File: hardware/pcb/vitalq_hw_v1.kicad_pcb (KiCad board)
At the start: 4 copper layers, 37 x 30 mm, 86 parts, among them J1 USB-C, J2 LiPo pads, J3 FSR pads, J4 PPG pads, J5 ECG pads, J6 EDA pads, U1 ESP32-WROOM-32E-N8R2, U10 AS7341-DLGM, U11 TMP117AIDRVR, U12 MLX90632SLD-DCB-100-SP, U13 BME280, U14 LSM6DSV80XTR, U2 MCP73831T-2ACI/OT, U3 XC6206P332MR-G, U4 TPS7A2018PDBVR, U5 CP2102N-A02-GQFN28R, U6 AFE4900YZR, U7 AD5940BCBZ-RL7, U8 ADS1292RIRSMT, U9 PCA9306DCUR

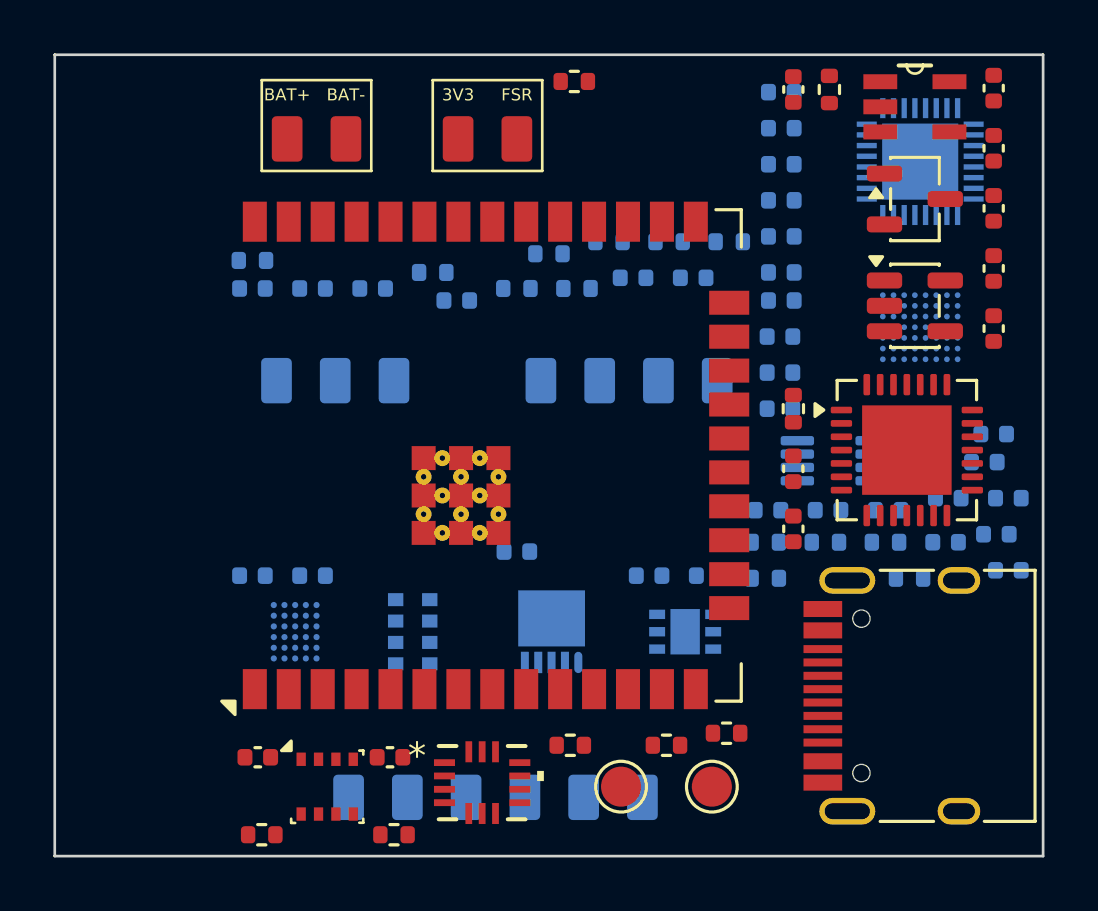
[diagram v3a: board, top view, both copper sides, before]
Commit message: Pack the hw_v1 board to 36.2 x 28 mm and correct the 3D models.
The LSM6 body is a 3.0 x 2.5 x 0.83 mm box in KiCad VRML units, and the other vendor models are rotated so they stand on their lands. Skin sensors sit in one bottom cluster with the electrode pads around them, bypass parts are packed next to their ICs outside the antenna keep-out, and the schematic frames clear the title block.

Co-authored-by: Riyu-D1 <Riyu-D1@users.noreply.github.com>
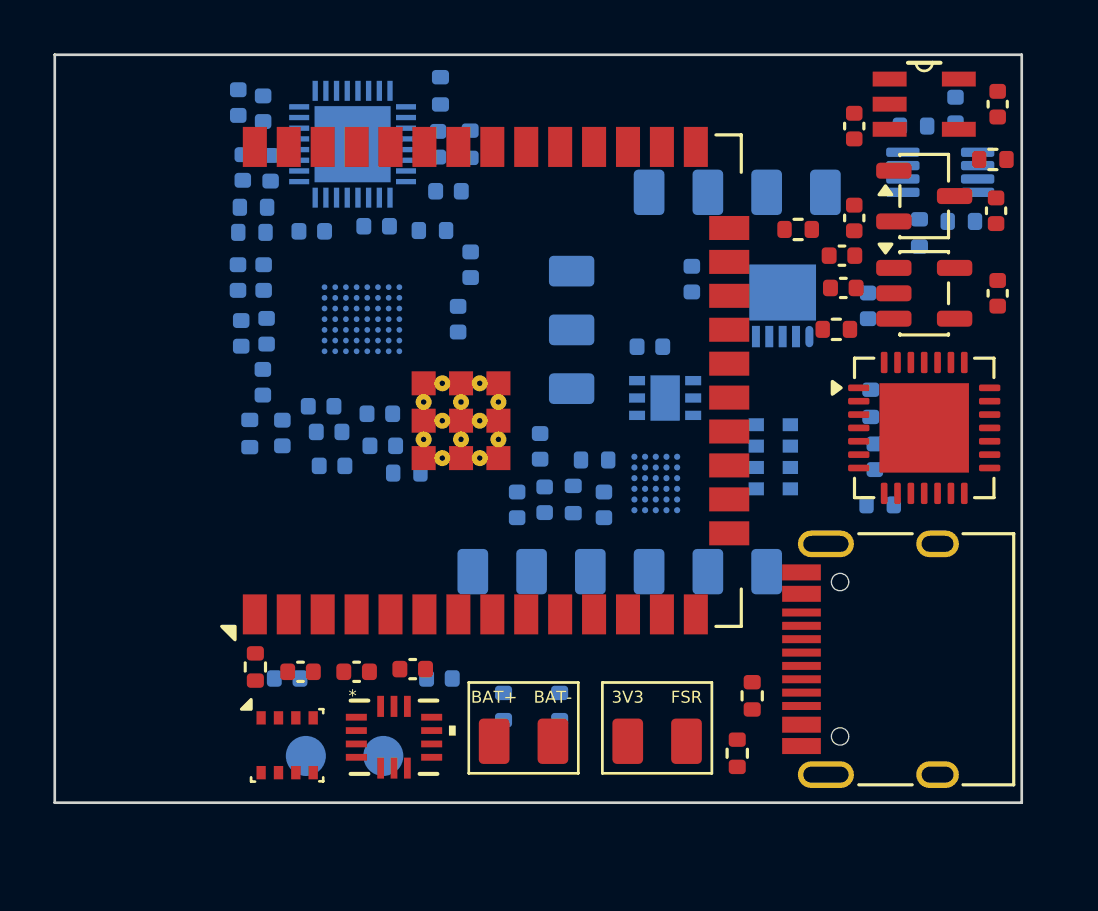
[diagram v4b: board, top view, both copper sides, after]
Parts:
- R6, R7, TP1, TP2: moved to B.Cu
- moved C20 30.0 mm to (7.82, 8.34), turned to 90 degrees
- moved C25 27.8 mm to (6.86, 8.34), turned to 90 degrees
- moved C26 27.3 mm to (8.52, 14.2), turned to 90 degrees
- moved R8 25.9 mm to (25.6, 26.1), turned to 90 degrees
- moved C21 25.3 mm to (10.3, 14.1)
- moved C5 25.2 mm to (13.4, 23.0), turned to 0 degrees
- moved R2 25.1 mm to (29.3, 10.3)
- moved J2 23.8 mm to (17.6, 25.7)
- moved J3 23.4 mm to (22.6, 25.7)
- moved C41 23.3 mm to (33.7, 2.07), turned to 90 degrees
- moved C38 23.1 mm to (30.4, 9.40), turned to 90 degrees
- moved C23 22.9 mm to (6.98, 10.4), turned to 90 degrees
- moved C27 22.2 mm to (10.4, 15.4)
- moved U8 21.3 mm to (11.2, 3.35)
- moved U7 20.9 mm to (11.5, 9.90)
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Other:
- board size 37 x 30 mm -> 36.2 x 28 mm

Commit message: Seat the QFN models and drop passives the datasheets do not require.
The ADS1292R STEP is already Z-up, so the extra X rotation stood the
4x4x1 mm body on edge. Remove TP1, TP2, C5, C12, C17, C31 and R4, add
the 1 uF AVDD bulk capacitor, and shorten the outline to 36.2 x 27.8 mm.

Co-authored-by: Riyu-D1 <Riyu-D1@users.noreply.github.com>
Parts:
- removed C12, C17, C31: 100n, Capacitor_SMD:C_0402_1005Metric
- removed C5: 1u, Capacitor_SMD:C_0402_1005Metric
- removed R4: 1k, Resistor_SMD:R_0402_1005Metric
- removed TP1: EN, TestPoint:TestPoint_Pad_D1.5mm
- removed TP2: IO0, TestPoint:TestPoint_Pad_D1.5mm
- added C43: 1u, Capacitor_SMD:C_0402_1005Metric, B.Cu at (12.1, 6.42)
- moved R16 4.41 mm to (17.2, 3.40)
- moved C29 2.10 mm to (14.1, 6.58)
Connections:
- U5 pad 9: CP_RST -> unconnected-(U5-~{RST}-Pad9)
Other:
- board size 36.2 x 28 mm -> 36.2 x 27.8 mm

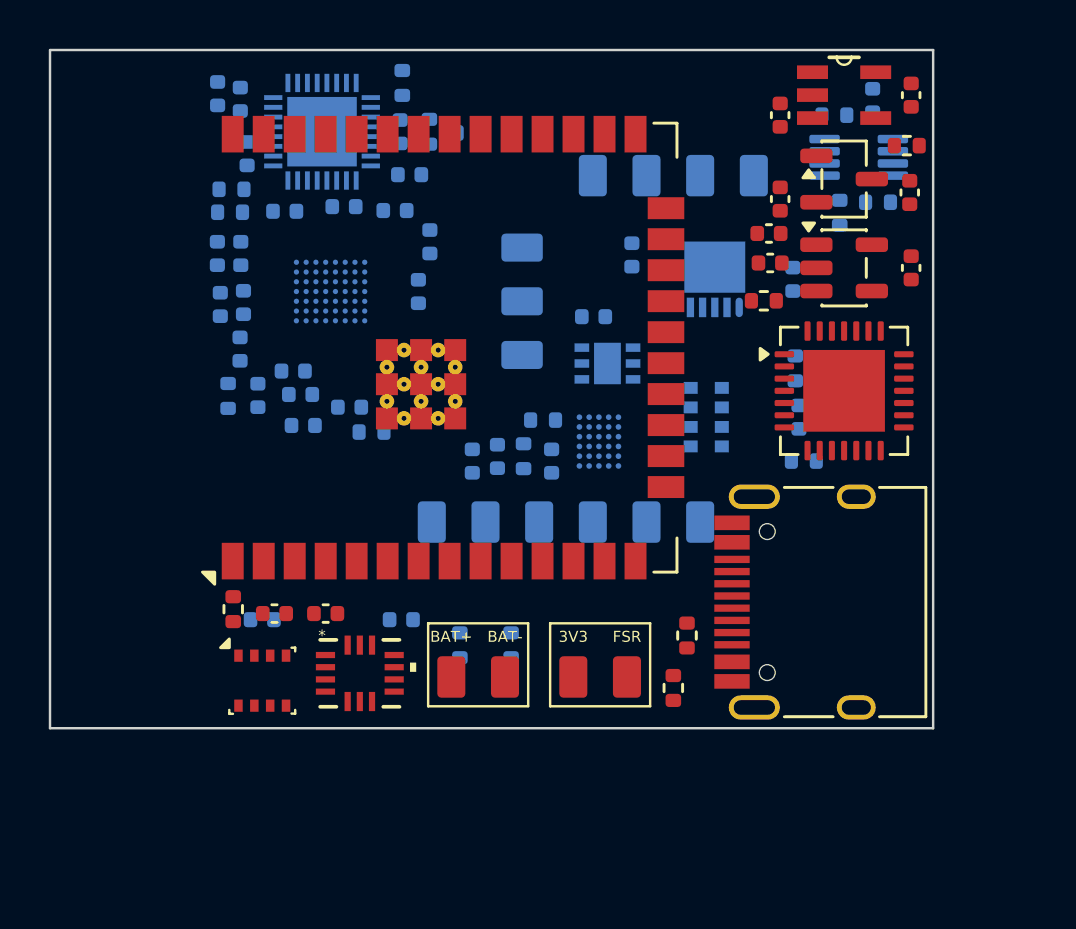
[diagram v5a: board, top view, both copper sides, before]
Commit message: Add the chest-board sensors and replace the 3.3 V LDO with a TPS63802.
The unrouted 40 x 34 mm board keeps every previous part except the off-board PPG pads, which the SFH 7072 replaces. Respiration, a second ECG lead, electrode protection, EDA, fuel gauge, flash, and the I/O expander are in the schematic.

Co-authored-by: Riyu-D1 <Riyu-D1@users.noreply.github.com>
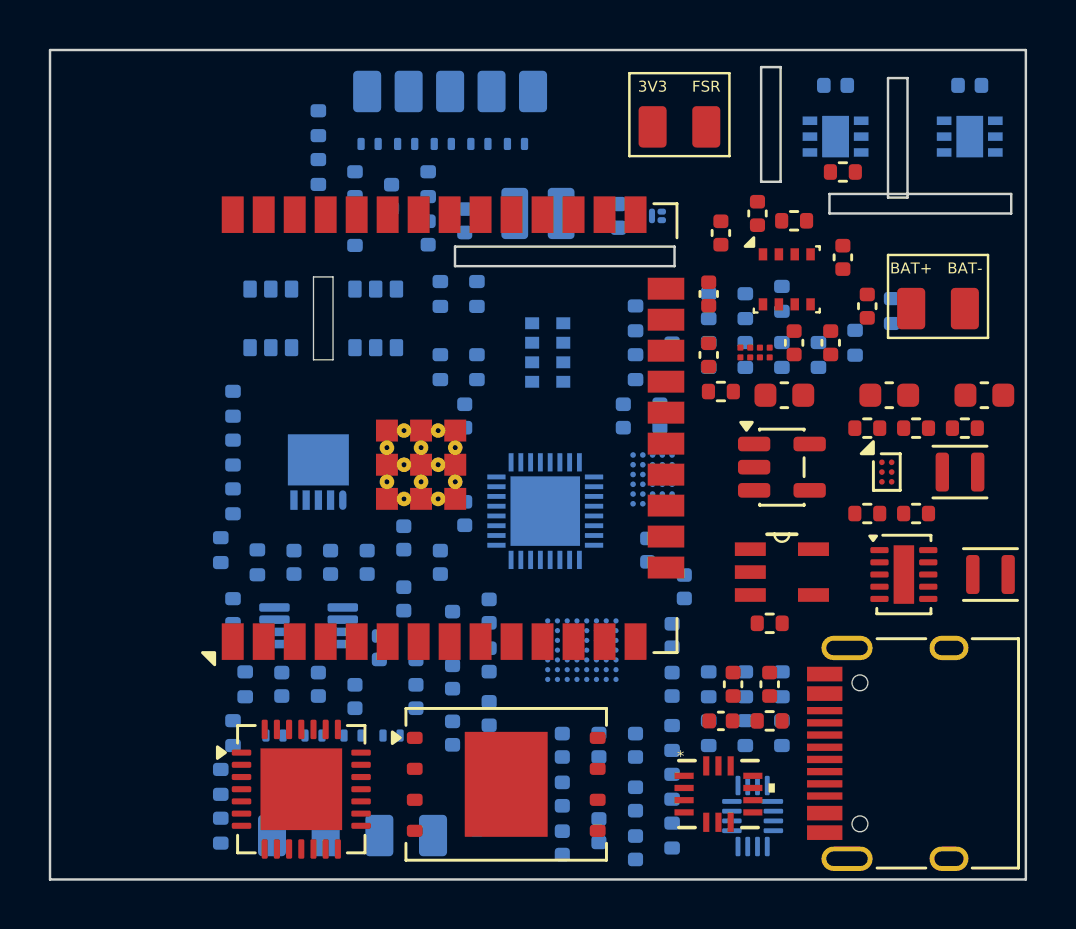
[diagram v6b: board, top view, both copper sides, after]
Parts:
- removed J4: PPG pads, vitalq:Pads_PPG
- added C44: 10u, Capacitor_SMD:C_0603_1608Metric, F.Cu at (30.1, 14.2)
- added C45: 22u, Capacitor_SMD:C_0603_1608Metric, F.Cu at (34.4, 14.2)
- added C46: 2.2u, Capacitor_SMD:C_0402_1005Metric, F.Cu at (32.5, 8.50)
- added C47: 4.7u, Capacitor_SMD:C_0603_1608Metric, F.Cu at (38.3, 14.2)
- added C48: 2.2n, Capacitor_SMD:C_0402_1005Metric, B.Cu at (11.0, 26.0)
- added C49: 2.2n, Capacitor_SMD:C_0402_1005Metric, B.Cu at (12.5, 26.5)
- added C50: 100n, Capacitor_SMD:C_0402_1005Metric, B.Cu at (17.0, 15.0)
- added C51: 100n, Capacitor_SMD:C_0402_1005Metric, B.Cu at (10.0, 21.0)
- added C52: 2.2n, Capacitor_SMD:C_0402_1005Metric, B.Cu at (9.50, 26.0)
- added C53: 2.2n, Capacitor_SMD:C_0402_1005Metric, B.Cu at (22.5, 28.5)
- added C54: 15n, Capacitor_SMD:C_0402_1005Metric, B.Cu at (21.0, 32.5)
- added C55: 470n, Capacitor_SMD:C_0402_1005Metric, B.Cu at (24.0, 28.5)
- added C56: 100n, Capacitor_SMD:C_0402_1005Metric, B.Cu at (25.0, 15.0)
- added C57: 100n, Capacitor_SMD:C_0402_1005Metric, B.Cu at (25.5, 26.0)
- added C58: 100n, Capacitor_SMD:C_0402_1005Metric, F.Cu at (27.5, 7.50)
- added C59: 100n, Capacitor_SMD:C_0402_1005Metric, B.Cu at (24.0, 30.7)
- added C60: 100n, Capacitor_SMD:C_0402_1005Metric, B.Cu at (24.0, 32.7)
- added C61: 100n, Capacitor_SMD:C_0402_1005Metric, B.Cu at (37.7, 1.45)
- added D1: TPD1E10B06, vitalq:TPD1E10B06_DPY, B.Cu at (13.1, 3.85)
- added D10: NF2W757G-F1, vitalq:NF2W757G, B.Cu at (20.0, 6.70)
- added D11: SFH4053, LED_SMD:LED_0402_1005Metric, B.Cu at (23.3, 6.80)
- added D2: TPD1E10B06, vitalq:TPD1E10B06_DPY, B.Cu at (14.6, 3.85)
- added D3: TPD1E10B06, vitalq:TPD1E10B06_DPY, B.Cu at (16.1, 3.85)
- added D4: TPD1E10B06, vitalq:TPD1E10B06_DPY, B.Cu at (17.6, 3.85)
- added D5: TPD1E10B06, vitalq:TPD1E10B06_DPY, B.Cu at (19.1, 3.85)
- added D6: TPD1E10B06, vitalq:TPD1E10B06_DPY, B.Cu at (9.20, 28.1)
- added D7: TPD1E10B06, vitalq:TPD1E10B06_DPY, B.Cu at (10.8, 28.1)
- added D8: TPD1E10B06, vitalq:TPD1E10B06_DPY, B.Cu at (12.4, 28.1)
- added D9: TPD1E10B06, vitalq:TPD1E10B06_DPY, B.Cu at (14.0, 28.1)
- added L1: 0.47u, vitalq:L_DFE201612E, F.Cu at (38.5, 21.5)
- added L2: 1.0u, vitalq:L_DFE201612E, F.Cu at (37.3, 17.3)
- added Q1: CSD13380F3, Package_DFN_QFN:Texas_PicoStar_DFN-3_0.69x0.60mm, B.Cu at (24.9, 6.80)
- added R23: 560k, Resistor_SMD:R_0402_1005Metric, F.Cu at (33.5, 19.0)
- added R24: 100k, Resistor_SMD:R_0402_1005Metric, F.Cu at (35.5, 19.0)
- added R25: 100k, Resistor_SMD:R_0402_1005Metric, F.Cu at (35.5, 15.5)
- added R26: 10M, Resistor_SMD:R_0402_1005Metric, B.Cu at (7.50, 16.5)
- added R27: 10M, Resistor_SMD:R_0402_1005Metric, B.Cu at (7.50, 18.5)
- added R28: 10M, Resistor_SMD:R_0402_1005Metric, B.Cu at (7.50, 23.0)
- added R29: 10M, Resistor_SMD:R_0402_1005Metric, B.Cu at (7.50, 28.0)
- added R30: 40.2k, Resistor_SMD:R_0402_1005Metric, B.Cu at (7.00, 30.0)
- added R31: 40.2k, Resistor_SMD:R_0402_1005Metric, B.Cu at (7.00, 20.5)
- added R32: 49.9k, Resistor_SMD:R_0402_1005Metric, B.Cu at (25.5, 11.5)
- added R33: 49.9k, Resistor_SMD:R_0402_1005Metric, B.Cu at (24.0, 11.0)
- added R34: 49.9k, Resistor_SMD:R_0402_1005Metric, B.Cu at (7.00, 32.0)
- added R35: 49.9k, Resistor_SMD:R_0402_1005Metric, B.Cu at (30.0, 26.0)
- added R36: 49.9k, Resistor_SMD:R_0402_1005Metric, B.Cu at (28.5, 28.0)
- added R39: 1k, Resistor_SMD:R_0402_1005Metric, B.Cu at (30.0, 28.0)
- added R40: 1k, Resistor_SMD:R_0402_1005Metric, B.Cu at (27.0, 12.5)
- added R41: 1k, Resistor_SMD:R_0402_1005Metric, B.Cu at (28.5, 12.5)
- added R42: 1k, Resistor_SMD:R_0402_1005Metric, B.Cu at (30.0, 12.5)
- added R43: 10M, Resistor_SMD:R_0402_1005Metric, B.Cu at (31.5, 12.5)
- added R44: 10M, Resistor_SMD:R_0402_1005Metric, B.Cu at (33.0, 12.0)
- added R45: 10M, Resistor_SMD:R_0402_1005Metric, B.Cu at (27.0, 10.5)
- added R46: 10M, Resistor_SMD:R_0402_1005Metric, B.Cu at (28.5, 10.5)
- added R47: 100, Resistor_SMD:R_0402_1005Metric, B.Cu at (11.0, 3.00)
- added R48: 100k, Resistor_SMD:R_0402_1005Metric, B.Cu at (11.0, 5.00)
- added R49: 10k, Resistor_SMD:R_0402_1005Metric, F.Cu at (27.5, 14.0)
- added R50: 100k, Resistor_SMD:R_0402_1005Metric, F.Cu at (30.5, 7.00)
- added R51: 200k, Resistor_SMD:R_0402_1005Metric, F.Cu at (37.5, 15.5)
- added R52: 10k, Resistor_SMD:R_0402_1005Metric, B.Cu at (34.5, 10.7)
- added R53: 10k, Resistor_SMD:R_0402_1005Metric, B.Cu at (30.0, 10.2)
- added U15: TPS61240YFFR, vitalq:TPS61240_YFF, F.Cu at (34.3, 17.3)
- added U16: SFH 7072, vitalq:SFH7072, B.Cu at (11.2, 11.0)
- added U17: MAX17048G+T10, vitalq:MAX17048_WLP, F.Cu at (28.9, 12.4)
- added U18: W25Q512JVEIQ, vitalq:W25Q512_WSON8, F.Cu at (18.7, 30.1)
- added U19: TCA6408ARSVR, vitalq:TCA6408A_RSV, B.Cu at (28.8, 31.4)
- added U20: TMP117AIDRVR, snap:SON65P200X200X80-7N, B.Cu at (37.7, 3.55)
- C37, C38: moved to F.Cu
- C7, C8, R5: moved to B.Cu
- U3: value XC6206P332MR-G -> TPS63802DLAR; footprint Package_TO_SOT_SMD:SOT-23-3 -> Package_SON:WSON-10-1EP_2x3mm_P0.5mm_EP0.84x2.4mm
- moved J6 30.1 mm to (12.4, 32.2)
- moved U9 29.6 mm to (10.6, 23.6)
- moved C40 28.2 mm to (32.2, 1.45)
- moved U5 27.6 mm to (10.3, 30.3)
- moved U13 27.1 mm to (30.2, 9.40)
- moved C25 25.9 mm to (19.5, 31.0)
- moved C42 25.1 mm to (22.5, 32.0)
- moved C1 24.8 mm to (29.5, 26.0)
- moved J2 24.2 mm to (36.4, 10.6)
- moved C33 23.3 mm to (18.0, 23.0)
- moved J3 22.8 mm to (25.8, 3.15)
- moved C22 22.5 mm to (21.0, 30.5)
- moved R8 22.3 mm to (32.5, 5.00), turned to 0 degrees
- moved C19 21.6 mm to (18.0, 29.5)
- moved R21 21.6 mm to (12.5, 5.50), turned to 90 degrees
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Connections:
- C14 pad 1: VBAT -> TX_5V
- J5 pad 1: IN1P -> ECG1_PAD
- J5 pad 2: IN1N -> ECG2_PAD
- J5 pad 3: RLDOUT -> RLD_PAD
- J6 pad 1: CE0 -> EDA_CE_PAD
- J6 pad 2: RE0 -> EDA_RE_PAD
- J6 pad 3: SE0 -> EDA_SE_PAD
- J6 pad 4: DE0 -> EDA_DE_PAD
- R11 pad 1: +3V3 -> AD5940_RESET
- R11 pad 2: AD5940_RESET -> GND
- R14 pad 1: +3V3 -> ADS1292_PWDN
- R14 pad 2: ADS1292_PWDN -> GND
- R9 pad 1: +3V3 -> AFE4900_RESETZ
- R9 pad 2: AFE4900_RESETZ -> GND
- U1 pad 10: ADS1292_PWDN -> unconnected-(U1-IO25-Pad10)
- U1 pad 11: ADS1292_START -> CS_FLASH
- U1 pad 12: AD5940_RESET -> unconnected-(U1-IO27-Pad12)
- U1 pad 28: AFE4900_RESETZ -> unconnected-(U1-IO17-Pad28)
- U1 pad 7: unconnected-(U1-IO35-Pad7) -> EXP_INT
- U10 pad 4: unconnected-(U10-LDR-Pad4) -> LDR
- U2 pad 1: unconnected-(U2-STAT-Pad1) -> CHG_STAT
- U3 pad 1: GND -> VBAT
- U3 pad 2: +3V3 -> GND
- U3 pad 3: VBAT -> GND
- U6 pad A1: unconnected-(U6-INM_ECG-PadA1) -> AFE_INM
- U6 pad B1: unconnected-(U6-INP_ECG-PadB1) -> AFE_INP
- U6 pad B2: unconnected-(U6-INP2-PadB2) -> PD2_INP
- U6 pad B3: unconnected-(U6-INM2-PadB3) -> PD2_INM
- U6 pad C5: unconnected-(U6-TX4-PadC5) -> TX4
- U6 pad F5: VBAT -> TX_5V
- U8 pad 16: ADS1292_START -> GND
- U8 pad 31: unconnected-(U8-RESP_MODP/IN3P-Pad31) -> RESP_MODP
- U8 pad 32: unconnected-(U8-RESP_MODN/IN3N-Pad32) -> RESP_MODN
- U8 pad 5: IN1N -> ECG_N
- U8 pad 6: IN1P -> ECG_P
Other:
- board size 36.2 x 27.8 mm -> 40 x 34 mm

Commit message: Cluster the skin sensors and set the respiration filter to 47 nF.
Stack U20 on top of U11, shrink the outline to 36.5 x 32 mm, and give the AFE4900 a generic WCSP body so it shows in the render.

Co-authored-by: Riyu-D1 <Riyu-D1@users.noreply.github.com>
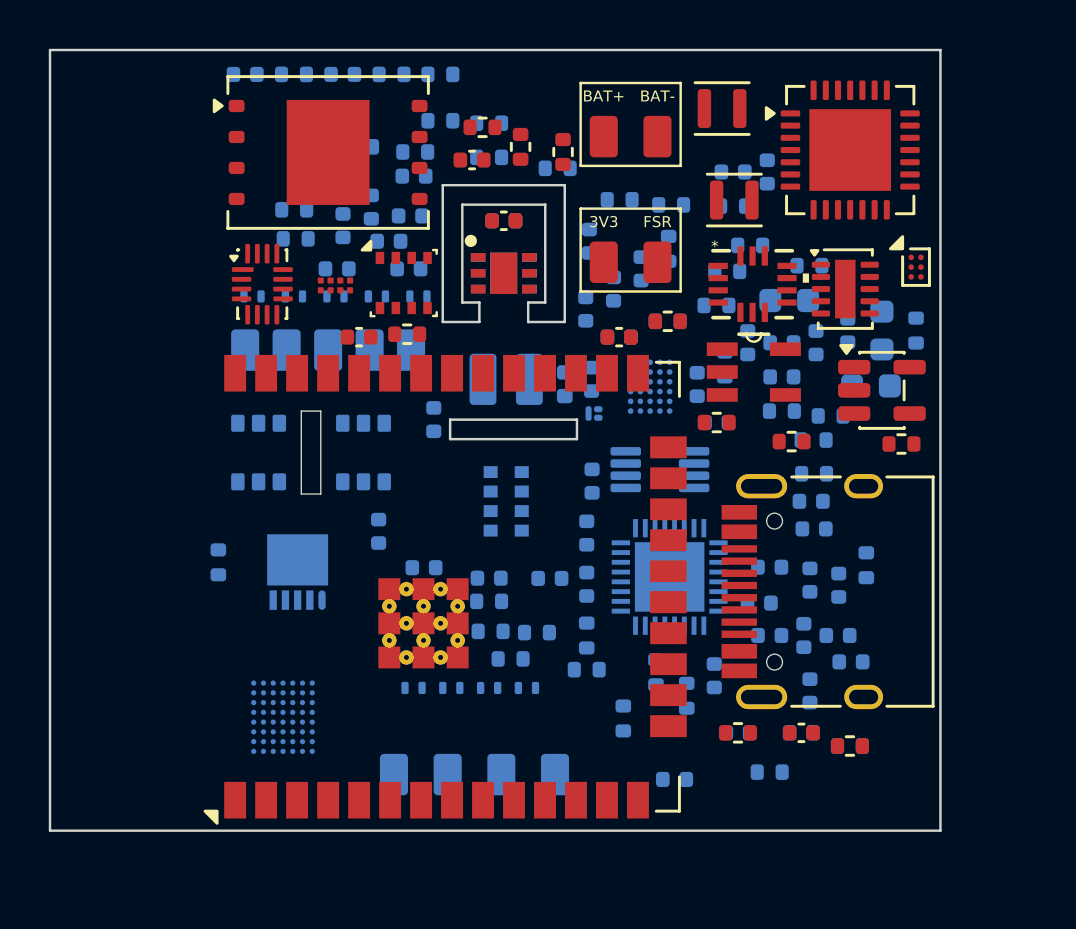
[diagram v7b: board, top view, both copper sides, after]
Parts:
- C1, C10, C2, C3, C37, C38, C4, C44, C45, C46, C47, C58, C6, R2, R23, R24, R25, R3, R50, R51, R8: moved to B.Cu
- C33, C43, C54, C61, R10, R11, R15, R31, R41, R44, R53, R6, U19, U20: moved to F.Cu
- C34: value 4.7n -> 47n
- moved U5 34.5 mm to (32.8, 4.10)
- moved R34 31.0 mm to (18.0, 3.00), turned to 180 degrees
- moved R7 30.0 mm to (10.0, 6.55), turned to 180 degrees
- moved U19 29.7 mm to (8.70, 9.60), turned to 0 degrees
- moved C60 28.4 mm to (13.2, 6.44)
- moved R5 27.4 mm to (12.7, 3.97), turned to 180 degrees
- moved R30 27.0 mm to (15.0, 4.18), turned to 180 degrees
- moved R6 27.0 mm to (19.3, 3.97)
- moved U18 26.9 mm to (11.4, 4.20)
- moved R48 25.7 mm to (23.5, 27.4)
- moved C59 25.6 mm to (14.8, 6.80), turned to 180 degrees
- moved R28 23.2 mm to (25.4, 8.15)
- moved C38 22.6 mm to (29.4, 5.00), turned to 90 degrees
- moved C7 22.2 mm to (14.9, 5.17), turned to 180 degrees
- moved L1 22.0 mm to (27.6, 2.40)
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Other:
- board size 40 x 34 mm -> 36.5 x 32 mm
